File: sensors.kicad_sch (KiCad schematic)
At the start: 11 parts, among them J3 Conn_01x03_Pin, J4 Conn_01x03_Pin, J5 Conn_01x03_Pin, J6 Conn_01x03_Pin, J7 Conn_01x04_Socket, U5 AHT20-F, U6 BMP581, U7 TLV493DA1B6HTSA2, U8 LSM6DS3TR-C

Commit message: add notes
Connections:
- net +ESC_5V: now reaches J3.3 (Pin_3)
- net +ESC_5V: now also J4.3 (Pin_3), J5.3 (Pin_3), J6.3 (Pin_3)
- no-connect marks 8 -> 4

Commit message: major overhaul
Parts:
- removed U5: AHT20-F, aht20f:SENSOR-SMD-6_AHT20, symbol aht20f:AHT20-F
- added J1, J9: Conn_01x07_Socket, Connector_PinHeader_2.54mm:PinHeader_1x07_P2.54mm_Vertical, symbol Connector:Conn_01x07_Socket
- added U1: AHT20-F, lib:SENSOR-SMD-6_AHT20, symbol lib:AHT20-F
- C27, C28: footprint (none) -> Capacitor_SMD:C_0402_1005Metric
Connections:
- net +3V3: now also U1.2 (VDD)
- net GND: now also J9.4 (Pin_4), U1.5 (GND)
- net NSS: now also J9.3 (Pin_3)
- net SCL: now also J9.1 (Pin_1), U1.3 (SCL)
- net SDA: now also J1.1 (Pin_1), U1.4 (SDA)
- new net +BATT: J1.4 (Pin_4)
- new net GPIO1: J1.5 (Pin_5)
- new net GPIO2: J9.5 (Pin_5)
- new net GPIO3: J1.6 (Pin_6)
- new net GPIO4: J9.6 (Pin_6)
- new net SPI_MISO: J1.2 (Pin_2)
- new net SPI_MOSI: J9.2 (Pin_2)
- new net SPI_SCK: J1.3 (Pin_3)
- new net VCC: J9.7 (Pin_7)
- new net WKUP1: J1.7 (Pin_7)

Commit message: working on placements
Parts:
- added SW2: TS-1187A-B-A-B, lib:SW-SMD_4P-L5.1-W5.1-P3.70-LS6.5-TL_H1.5, symbol lib:TS-1187A-B-A-B
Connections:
- net GND: now also SW2.3 (C), SW2.4 (D)
- new net DEBUG_BTN_1: SW2.1 (A), SW2.2 (B)
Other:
- note added: "For setting GPS position"

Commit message: nearly there
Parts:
- J1, J3, J4, J5, J7, J9: now left out of the parts list
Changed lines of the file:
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@@
 		(unit 1)
 		(exclude_from_sim no)
-		(in_bom yes)
+		(in_bom no)
 		(on_board yes)
 		(dnp no)
@@
 		(unit 1)
 		(exclude_from_sim no)
-		(in_bom yes)
+		(in_bom no)
 		(on_board yes)
 		(dnp no)
@@
 		(unit 1)
 		(exclude_from_sim no)
-		(in_bom yes)
+		(in_bom no)
 		(on_board yes)
 		(dnp no)
@@
 		(unit 1)
 		(exclude_from_sim no)
-		(in_bom yes)
+		(in_bom no)
 		(on_board yes)
 		(dnp no)
@@
 		(unit 1)
 		(exclude_from_sim no)
-		(in_bom yes)
+		(in_bom no)
 		(on_board yes)
 		(dnp no)
@@
 		(unit 1)
 		(exclude_from_sim no)
-		(in_bom yes)
+		(in_bom no)
 		(on_board yes)
 		(dnp no)

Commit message: prod1
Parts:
- removed C27, C28: 100nF, Capacitor_SMD:C_0402_1005Metric, symbol Device:C
- removed U6: BMP581, lib:LGA-10_L2.0-W2.0-P0.50-TL_BMP581, symbol lib:BMP581
- removed U8: LSM6DS3TR-C, lib:LGA-14_L3.0-W2.5-P0.50-TL, symbol lib:LSM6DS3TR-C
- added C5: 10nF, Capacitor_SMD:C_0402_1005Metric, symbol Device:C
- added C6: 100nF, Capacitor_SMD:C_0402_1005Metric, symbol Device:C
- added U3: ICM-42688-P, lib2:LGA-14_L3.0-W2.5-P0.50-TL, symbol lib2:ICM-42688-P
- added U4: GZP6816D, lib2:SENSOR-SMD_XGZP6816D, symbol lib2:GZP6816D
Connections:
- net +3V3: now also C5.1, C6.1, U3.12 (AP_CS), U3.5 (VDDIO), U3.8 (VDD), U4.8 (VDD)
- net GND: now also C5.2, C6.2, U3.1 (AP_SDO/AP_AD0), U3.10 (RESV), U3.11 (RESV), U3.2 (RESV), U3.3 (RESV), U3.6 (GND), U3.7 (RESV), U4.1 (GND), U4.7 (GND)
- net LSM6_INT1: now also U3.4 (INT1/INT)
- net LSM6_INT2: now also U3.9 (INT2/FSYNC/CLKIN)
- net SCL: now also U3.13 (AP_SCL/AP_SCLK), U4.4 (SCL)
- net SDA: now also U3.14 (AP_SDA/AP_SDIO/AP_SDI), U4.3 (SDA)
- no-connect marks 4 -> 5
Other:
- note removed: "PRESSURE"

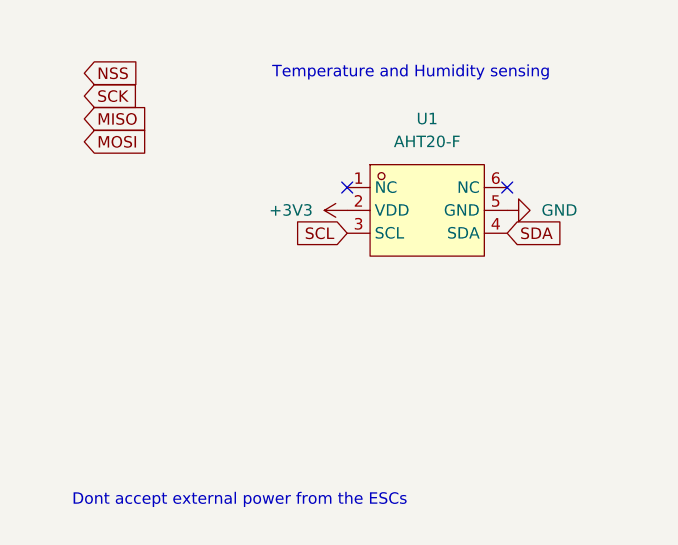
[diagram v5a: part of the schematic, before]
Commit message: fix issues with power supply
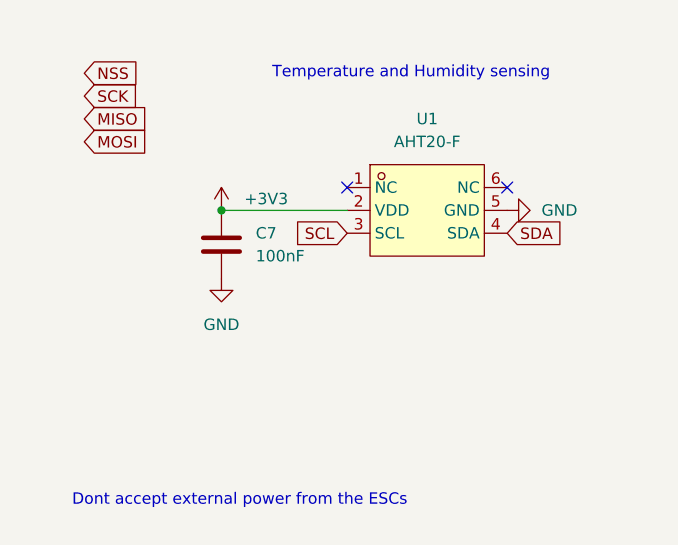
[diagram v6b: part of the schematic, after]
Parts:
- added C7: 100nF, Capacitor_SMD:C_0402_1005Metric, symbol Device:C
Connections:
- net +3V3: now also C7.1
- net GND: now also C7.2
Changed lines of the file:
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@@
 	(paper "A4")
 	(junction
+		(at 38.1 35.56)
+		(diameter 0)
+		(color 0 0 0 0)
+	)
+	(junction
 		(at 255.27 99.06)
 		(diameter 0)
@@
 	(wire
 		(pts
+			(xy 38.1 35.56) (xy 52.07 35.56)
+		)
+		(stroke
+			(width 0)
+			(type default)
+		)
+	)
+	(wire
+		(pts
 			(xy 128.27 31.75) (xy 128.27 36.83)
 		)
@@
 	)
 	(symbol
+		(lib_id "Device:C")
+		(at 38.1 39.37 0)
+		(unit 1)
+		(exclude_from_sim no)
+		(in_bom yes)
+		(on_board yes)
+		(dnp no)
+		(fields_autoplaced yes)
+		(property "Reference" "C7"
+			(at 41.91 38.0999 0)
+			(effects
+				(font
+					(size 1.27 1.27)
+				)
+				(justify left)
+			)
+		)
+		(property "Value" "100nF"
+			(at 41.91 40.6399 0)
+			(effects
+				(font
+					(size 1.27 1.27)
+				)
+				(justify left)
+			)
+		)
+		(property "Footprint" "Capacitor_SMD:C_0402_1005Metric"
+			(at 39.0652 43.18 0)
+			(effects
+				(font
+					(size 1.27 1.27)
+				)
+				(hide yes)
+			)
+		)
+		(property "Datasheet" "~"
+			(at 38.1 39.37 0)
+			(effects
+				(font
+					(size 1.27 1.27)
+				)
+				(hide yes)
+			)
+		)
+		(property "Description" "Unpolarized capacitor"
+			(at 38.1 39.37 0)
+			(effects
+				(font
+					(size 1.27 1.27)
+				)
+				(hide yes)
+			)
+		)
+		(pin "2"
+		)
+		(pin "1"
+		)
+		(instances
+			(project "RTLS_VIC"
+				(path "/52945f31-6668-4093-a729-6e60f954b598/3943121a-fa5d-4ebf-b59e-9c4b09bc85dd"
+					(reference "C7")
+					(unit 1)
+				)
+			)
+		)
+	)
+	(symbol
 		(lib_id "power:GND")
 		(at 49.53 109.22 270)
@@
 	(symbol
 		(lib_id "power:+3V3")
-		(at 52.07 35.56 90)
+		(at 38.1 35.56 0)
 		(unit 1)
 		(exclude_from_sim no)
@@
 		(fields_autoplaced yes)
 		(property "Reference" "#PWR043"
-			(at 55.88 35.56 0)
+			(at 38.1 39.37 0)
 			(effects
 				(font
@@
 		)
 		(property "Value" "+3V3"
-			(at 48.26 35.5599 90)
+			(at 40.64 34.2899 0)
 			(effects
 				(font
@@
 		)
 		(property "Footprint" ""
-			(at 52.07 35.56 0)
+			(at 38.1 35.56 0)
 			(effects
 				(font
@@
 		)
 		(property "Datasheet" ""
-			(at 52.07 35.56 0)
+			(at 38.1 35.56 0)
 			(effects
 				(font
@@
 		)
 		(property "Description" "Power symbol creates a global label with name \"+3V3\""
-			(at 52.07 35.56 0)
+			(at 38.1 35.56 0)
 			(effects
 				(font
@@
 					(unit 1)
 				)
+			)
+		)
+	)
+	(symbol
+		(lib_id "power:GND")
+		(at 38.1 43.18 0)
+		(unit 1)
+		(exclude_from_sim no)
+		(in_bom yes)
+		(on_board yes)
+		(dnp no)
+		(fields_autoplaced yes)
+		(property "Reference" "#PWR053"
+			(at 38.1 49.53 0)
+			(effects
+				(font
+					(size 1.27 1.27)
+				)
+				(hide yes)
+			)
+		)
+		(property "Value" "GND"
+			(at 38.1 48.26 0)
+			(effects
+				(font
+					(size 1.27 1.27)
+				)
+			)
+		)
+		(property "Footprint" ""
+			(at 38.1 43.18 0)
+			(effects
+				(font
+					(size 1.27 1.27)
+				)
+				(hide yes)
+			)
+		)
+		(property "Datasheet" ""
+			(at 38.1 43.18 0)
+			(effects
+				(font
+					(size 1.27 1.27)
+				)
+				(hide yes)
+			)
+		)
+		(property "Description" "Power symbol creates a global label with name \"GND\" , ground"
+			(at 38.1 43.18 0)
+			(effects
+				(font
+					(size 1.27 1.27)
+				)
+				(hide yes)
+			)
+		)
+		(pin "1"
+		)
+		(instances
+			(project "RTLS_VIC"
+				(path "/52945f31-6668-4093-a729-6e60f954b598/3943121a-fa5d-4ebf-b59e-9c4b09bc85dd"
+					(reference "#PWR053")
+					(unit 1)
+				)

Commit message: initial boom arm cad and sim
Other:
- note added: "Do accept external power from the ESCs"
- note added: "in future revision, the PWM pins must go SIG POW GND"
- note removed: "Dont accept external power from the ESCs"
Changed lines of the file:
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@@
+		)
+	)
+	(text "in future revision, the PWM pins must go SIG POW GND"
+		(exclude_from_sim no)
+		(at 35.306 71.374 0)
+		(effects
+			(font
+				(size 1.27 1.27)
+			)
 		)
 	)
@@
 		)
 	)
-	(text "Dont accept external power from the ESCs"
+	(text "Do accept external power from the ESCs"
 		(exclude_from_sim no)
 		(at 40.132 67.818 0)
